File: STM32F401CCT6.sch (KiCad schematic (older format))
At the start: 42 parts, among them J1 USB_OTG, J2 Conn_02x03_Odd_Even, J3 Conn_01x20_des, J4 Conn_01x05_desc, J5 Conn_01x20, SW1 SW_Push, U1 MIC5219-3.3, U3 USBLC6-2SC6, Y1 32.786K, Y2 8MHz

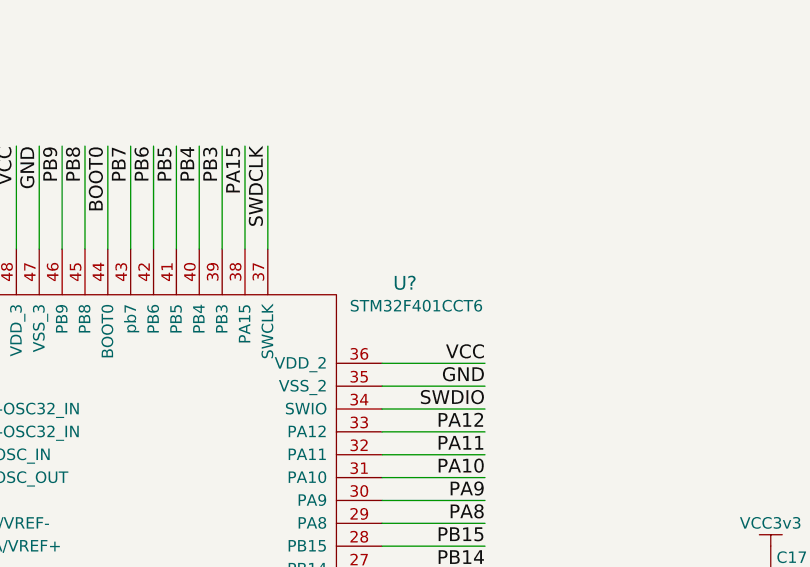
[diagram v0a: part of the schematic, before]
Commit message: Fixed the pad near tracks error (reallocated the QFN)
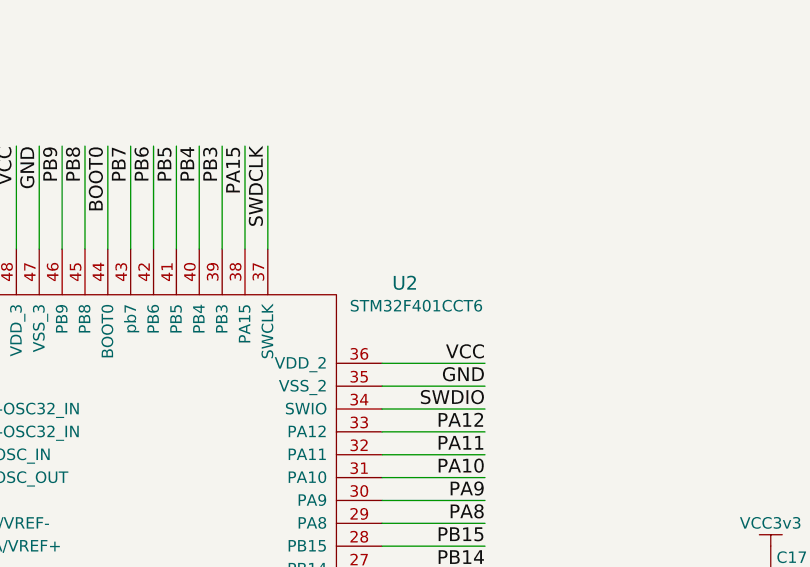
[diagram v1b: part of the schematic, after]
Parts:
- gave numbers to parts that had none: 1
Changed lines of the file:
@@
 $EndComp
 $Comp
-L GND #PWR01
+L GND #PWR9
 U 1 1 59D25E0A
 P 2500 1550
-F 0 "#PWR01" H 2500 1300 50  0001 C CNN
+F 0 "#PWR9" H 2500 1300 50  0001 C CNN
 F 1 "GND" H 2500 1400 50  0000 C CNN
 F 2 "" H 2500 1550 50  0001 C CNN
@@
 $EndComp
 $Comp
-L VCC3v3 #PWR02
+L VCC3v3 #PWR16
 U 1 1 59D2614B
 P 4700 850
-F 0 "#PWR02" H 4700 700 50  0001 C CNN
+F 0 "#PWR16" H 4700 700 50  0001 C CNN
 F 1 "VCC3v3" H 4700 950 50  0000 C CNN
 F 2 "" H 4700 850 50  0001 C CNN
@@
 $EndComp
 $Comp
-L VCC3v3 #PWR03
+L VCC3v3 #PWR17
 U 1 1 59D261AF
 P 4700 1350
-F 0 "#PWR03" H 4700 1200 50  0001 C CNN
+F 0 "#PWR17" H 4700 1200 50  0001 C CNN
 F 1 "VCC3v3" H 4700 1450 50  0000 C CNN
 F 2 "" H 4700 1350 50  0001 C CNN
@@
 $EndComp
 $Comp
-L VCC3v3 #PWR04
+L VCC3v3 #PWR13
 U 1 1 59D261DA
 P 3000 900
-F 0 "#PWR04" H 3000 750 50  0001 C CNN
+F 0 "#PWR13" H 3000 750 50  0001 C CNN
 F 1 "VCC3v3" H 3000 1000 50  0000 C CNN
 F 2 "" H 3000 900 50  0001 C CNN
@@
 BOOT0
 $Comp
-L VCC3v3 #PWR05
+L VCC3v3 #PWR2
 U 1 1 59D2665A
 P 1050 900
-F 0 "#PWR05" H 1050 750 50  0001 C CNN
+F 0 "#PWR2" H 1050 750 50  0001 C CNN
 F 1 "VCC3v3" H 1050 1000 50  0000 C CNN
 F 2 "" H 1050 900 50  0001 C CNN
@@
 RESET
 $Comp
-L GND #PWR06
+L GND #PWR3
 U 1 1 59D2716C
 P 1050 1950
-F 0 "#PWR06" H 1050 1700 50  0001 C CNN
+F 0 "#PWR3" H 1050 1700 50  0001 C CNN
 F 1 "GND" H 1050 1800 50  0000 C CNN
 F 2 "" H 1050 1950 50  0001 C CNN
@@
 $EndComp
 $Comp
-L 5V #PWR07
+L 5V #PWR6
 U 1 1 59D2797D
 P 1700 5900
-F 0 "#PWR07" H 1700 5750 50  0001 C CNN
+F 0 "#PWR6" H 1700 5750 50  0001 C CNN
 F 1 "5V" H 1700 6040 50  0000 C CNN
 F 2 "" H 1700 5900 50  0001 C CNN
@@
 $EndComp
 $Comp
-L VCC3v3 #PWR08
+L VCC3v3 #PWR7
 U 1 1 59D27D4D
 P 2150 6900
-F 0 "#PWR08" H 2150 6750 50  0001 C CNN
+F 0 "#PWR7" H 2150 6750 50  0001 C CNN
 F 1 "VCC3v3" H 2150 7000 50  0000 C CNN
 F 2 "" H 2150 6900 50  0001 C CNN
@@
 $EndComp
 $Comp
-L GND #PWR09
+L GND #PWR15
 U 1 1 59D289B6
 P 3750 5700
-F 0 "#PWR09" H 3750 5450 50  0001 C CNN
+F 0 "#PWR15" H 3750 5450 50  0001 C CNN
 F 1 "GND" H 3750 5550 50  0000 C CNN
 F 2 "" H 3750 5700 50  0001 C CNN
@@
 $EndComp
 $Comp
-L VCC3v3 #PWR010
+L VCC3v3 #PWR28
 U 1 1 59D28DD5
 P 10200 5450
-F 0 "#PWR010" H 10200 5300 50  0001 C CNN
+F 0 "#PWR28" H 10200 5300 50  0001 C CNN
 F 1 "VCC3v3" H 10200 5550 50  0000 C CNN
 F 2 "" H 10200 5450 50  0001 C CNN
@@
 $EndComp
 $Comp
-L GND #PWR011
+L GND #PWR29
 U 1 1 59D28EE2
 P 10200 5950
-F 0 "#PWR011" H 10200 5700 50  0001 C CNN
+F 0 "#PWR29" H 10200 5700 50  0001 C CNN
 F 1 "GND" H 10200 5800 50  0000 C CNN
 F 2 "" H 10200 5950 50  0001 C CNN
@@
 $EndComp
 $Comp
-L VCC3v3 #PWR012
+L VCC3v3 #PWR26
 U 1 1 59D2CC11
 P 9850 4400
-F 0 "#PWR012" H 9850 4250 50  0001 C CNN
+F 0 "#PWR26" H 9850 4250 50  0001 C CNN
 F 1 "VCC3v3" H 9850 4500 50  0000 C CNN
 F 2 "" H 9850 4400 50  0001 C CNN
@@
 $EndComp
 $Comp
-L GND #PWR013
+L GND #PWR27
 U 1 1 59D2CC17
 P 9850 4700
-F 0 "#PWR013" H 9850 4450 50  0001 C CNN
+F 0 "#PWR27" H 9850 4450 50  0001 C CNN
 F 1 "GND" H 9850 4550 50  0000 C CNN
 F 2 "" H 9850 4700 50  0001 C CNN
@@
 $EndComp
 $Comp
-L VCC3v3 #PWR014
+L VCC3v3 #PWR30
 U 1 1 59D2CC94
 P 10300 4400
-F 0 "#PWR014" H 10300 4250 50  0001 C CNN
+F 0 "#PWR30" H 10300 4250 50  0001 C CNN
 F 1 "VCC3v3" H 10300 4500 50  0000 C CNN
 F 2 "" H 10300 4400 50  0001 C CNN
@@
 $EndComp
 $Comp
-L GND #PWR015
+L GND #PWR31
 U 1 1 59D2CC9A
 P 10300 4700
-F 0 "#PWR015" H 10300 4450 50  0001 C CNN
+F 0 "#PWR31" H 10300 4450 50  0001 C CNN
 F 1 "GND" H 10300 4550 50  0000 C CNN
 F 2 "" H 10300 4700 50  0001 C CNN
@@
 $EndComp
 $Comp
-L GND #PWR016
+L GND #PWR5
 U 1 1 59D2D880
 P 1650 6750
-F 0 "#PWR016" H 1650 6500 50  0001 C CNN
+F 0 "#PWR5" H 1650 6500 50  0001 C CNN
 F 1 "GND" H 1650 6600 50  0000 C CNN
 F 2 "" H 1650 6750 50  0001 C CNN
@@
 $EndComp
 $Comp
-L GND #PWR017
+L GND #PWR1
 U 1 1 59D37486
 P 750 4400
-F 0 "#PWR017" H 750 4150 50  0001 C CNN
+F 0 "#PWR1" H 750 4150 50  0001 C CNN
 F 1 "GND" H 750 4250 50  0000 C CNN
 F 2 "" H 750 4400 50  0001 C CNN
@@
 $EndComp
 $Comp
-L 5V #PWR018
+L 5V #PWR4
 U 1 1 59D374F7
 P 1300 3500
-F 0 "#PWR018" H 1300 3350 50  0001 C CNN
+F 0 "#PWR4" H 1300 3350 50  0001 C CNN
 F 1 "5V" H 1300 3640 50  0000 C CNN
 F 2 "" H 1300 3500 50  0001 C CNN
@@
 $EndComp
 $Comp
-L VCC3v3 #PWR019
+L VCC3v3 #PWR10
 U 1 1 59D376BC
 P 2600 3550
-F 0 "#PWR019" H 2600 3400 50  0001 C CNN
+F 0 "#PWR10" H 2600 3400 50  0001 C CNN
 F 1 "VCC3v3" H 2600 3650 50  0000 C CNN
 F 2 "" H 2600 3550 50  0001 C CNN
@@
 $EndComp
 $Comp
-L GND #PWR020
+L GND #PWR11
 U 1 1 59D37C81
 P 2600 4350
-F 0 "#PWR020" H 2600 4100 50  0001 C CNN
+F 0 "#PWR11" H 2600 4100 50  0001 C CNN
 F 1 "GND" H 2600 4200 50  0000 C CNN
 F 2 "" H 2600 4350 50  0001 C CNN
@@
 $EndComp
 $Comp
-L GND #PWR021
+L GND #PWR12
 U 1 1 59D37D1C
 P 2950 4350
-F 0 "#PWR021" H 2950 4100 50  0001 C CNN
+F 0 "#PWR12" H 2950 4100 50  0001 C CNN
 F 1 "GND" H 2950 4200 50  0000 C CNN
 F 2 "" H 2950 4350 50  0001 C CNN
@@
 $EndComp
 $Comp
-L GND #PWR022
+L GND #PWR21
 U 1 1 59D379C4
 P 8700 900
-F 0 "#PWR022" H 8700 650 50  0001 C CNN
+F 0 "#PWR21" H 8700 650 50  0001 C CNN
 F 1 "GND" H 8700 750 50  0000 C CNN
 F 2 "" H 8700 900 50  0001 C CNN
@@
 $EndComp
 $Comp
-L VCC3v3 #PWR023
+L VCC3v3 #PWR14
 U 1 1 59D3C6B3
 P 3250 6850
-F 0 "#PWR023" H 3250 6700 50  0001 C CNN
+F 0 "#PWR14" H 3250 6700 50  0001 C CNN
 F 1 "VCC3v3" H 3250 6950 50  0000 C CNN
 F 2 "" H 3250 6850 50  0001 C CNN
@@
 $EndComp
 $Comp
-L GND #PWR024
+L GND #PWR8
 U 1 1 59D3C918
 P 2450 6850
-F 0 "#PWR024" H 2450 6600 50  0001 C CNN
+F 0 "#PWR8" H 2450 6600 50  0001 C CNN
 F 1 "GND" H 2450 6700 50  0000 C CNN
 F 2 "" H 2450 6850 50  0001 C CNN
@@
 PB11/VCAP1
 $Comp
-L GND #PWR025
+L GND #PWR18
 U 1 1 59FD831D
 P 6450 6150
-F 0 "#PWR025" H 6450 5900 50  0001 C CNN
+F 0 "#PWR18" H 6450 5900 50  0001 C CNN
 F 1 "GND" H 6450 6000 50  0000 C CNN
 F 2 "" H 6450 6150 50  0001 C CNN
@@
 $EndComp
 $Comp
-L VCC3v3 #PWR026
+L VCC3v3 #PWR19
 U 1 1 5A0064CD
 P 8400 5450
-F 0 "#PWR026" H 8400 5300 50  0001 C CNN
+F 0 "#PWR19" H 8400 5300 50  0001 C CNN
 F 1 "VCC3v3" H 8400 5550 50  0000 C CNN
 F 2 "" H 8400 5450 50  0001 C CNN
@@
 $EndComp
 $Comp
-L GND #PWR027
+L GND #PWR20
 U 1 1 5A0064D3
 P 8400 5950
-F 0 "#PWR027" H 8400 5700 50  0001 C CNN
+F 0 "#PWR20" H 8400 5700 50  0001 C CNN
 F 1 "GND" H 8400 5800 50  0000 C CNN
 F 2 "" H 8400 5950 50  0001 C CNN
@@
 $EndComp
 $Comp
-L VCC3v3 #PWR028
+L VCC3v3 #PWR24
 U 1 1 5A006C48
 P 9350 4400
-F 0 "#PWR028" H 9350 4250 50  0001 C CNN
+F 0 "#PWR24" H 9350 4250 50  0001 C CNN
 F 1 "VCC3v3" H 9350 4500 50  0000 C CNN
 F 2 "" H 9350 4400 50  0001 C CNN
@@
 $EndComp
 $Comp
-L GND #PWR029
+L GND #PWR25
 U 1 1 5A006C4E
 P 9350 4700
-F 0 "#PWR029" H 9350 4450 50  0001 C CNN
+F 0 "#PWR25" H 9350 4450 50  0001 C CNN
 F 1 "GND" H 9350 4550 50  0000 C CNN
 F 2 "" H 9350 4700 50  0001 C CNN
@@
 $EndComp
 $Comp
-L VCC3v3 #PWR030
+L VCC3v3 #PWR22
 U 1 1 5A006D31
 P 8850 4400
-F 0 "#PWR030" H 8850 4250 50  0001 C CNN
+F 0 "#PWR22" H 8850 4250 50  0001 C CNN
 F 1 "VCC3v3" H 8850 4500 50  0000 C CNN
 F 2 "" H 8850 4400 50  0001 C CNN
@@
 $EndComp
 $Comp
-L GND #PWR031
+L GND #PWR23
 U 1 1 5A006D37
 P 8850 4700
-F 0 "#PWR031" H 8850 4450 50  0001 C CNN
+F 0 "#PWR23" H 8850 4450 50  0001 C CNN
 F 1 "GND" H 8850 4550 50  0000 C CNN
 F 2 "" H 8850 4700 50  0001 C CNN
@@
 $EndComp
 $Comp
-L STM32F401CCT6 U?
+L STM32F401CCT6 U2
 U 1 1 5A00751A
 P 5700 3850
-F 0 "U?" H 7250 4450 60  0000 C CNN
+F 0 "U2" H 7250 4450 60  0000 C CNN
 F 1 "STM32F401CCT6" H 7300 4350 50  0000 C CNN
 F 2 "" H 5700 3850 60  0001 C CNN

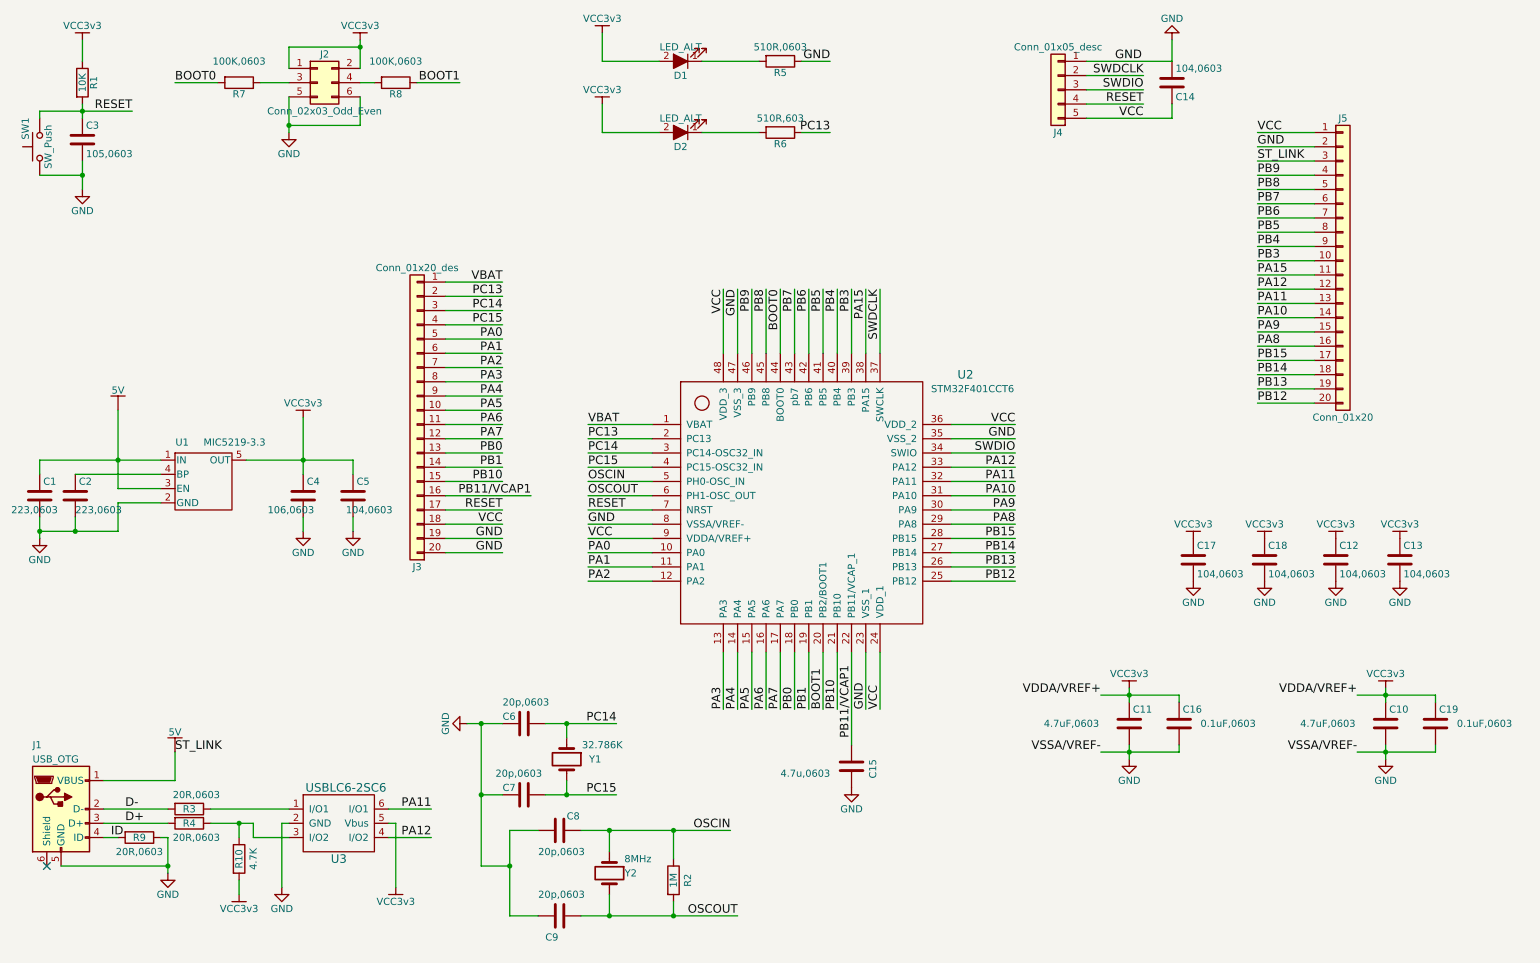
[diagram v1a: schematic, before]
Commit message: Change pin20 to Pwr Enable and added a resistor on it
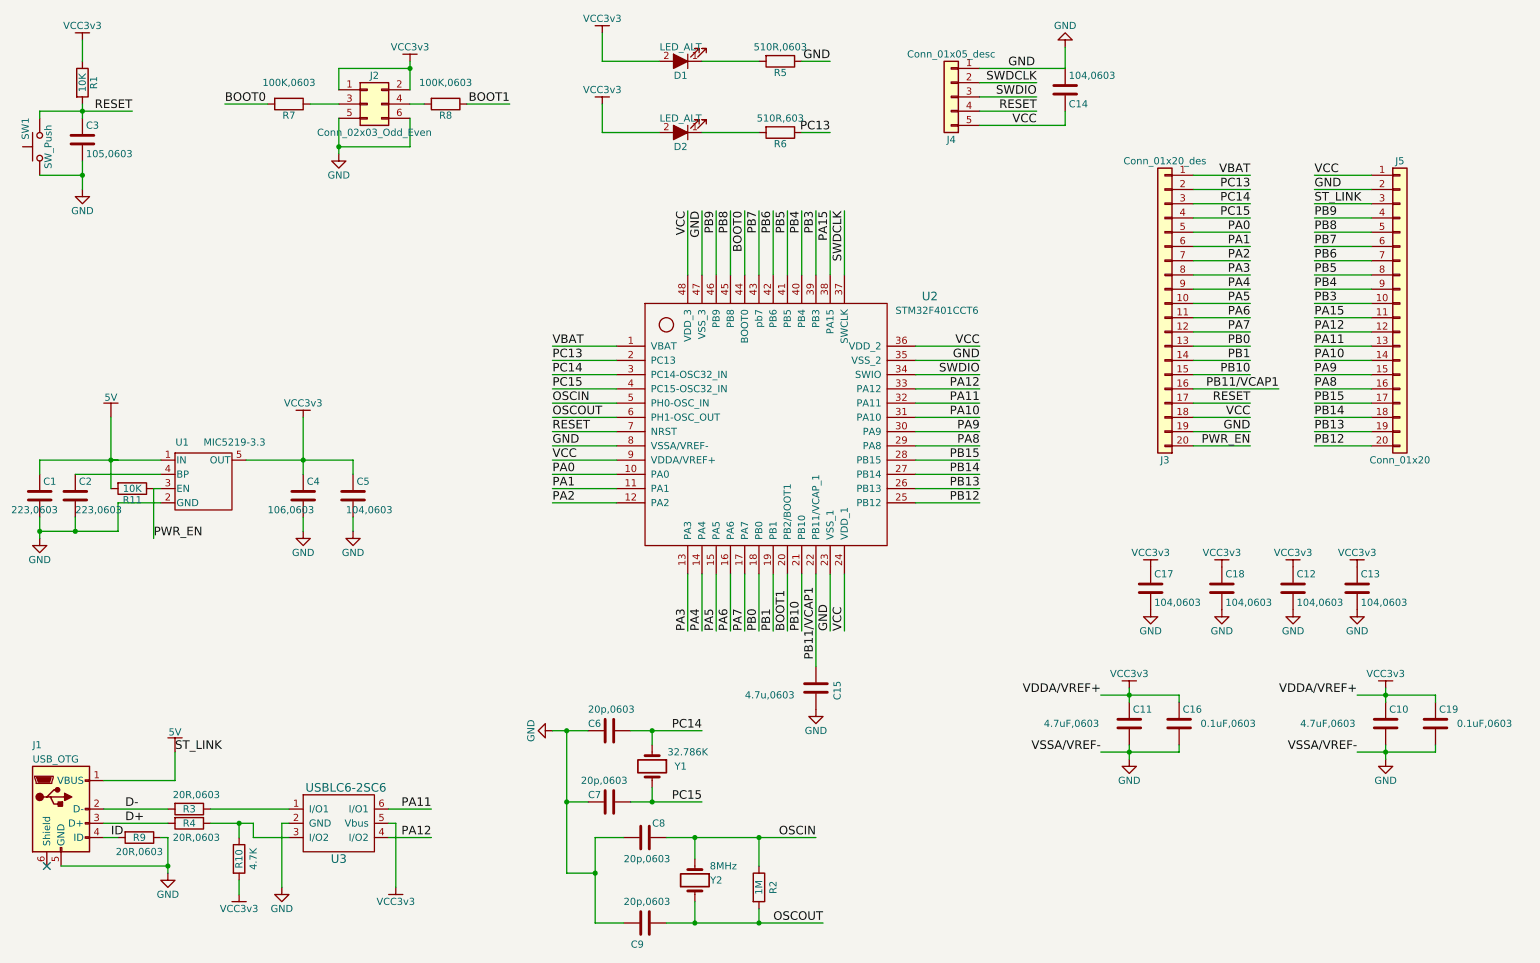
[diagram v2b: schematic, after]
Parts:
- added R11: 10K, Resistors_SMD:R_0603, symbol R
- U2: footprint (none) -> QFPN48:QFN_QFP48
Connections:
- net +5V: now also R11.2; no longer U1.3 (EN)
- net GND: no longer J3.20 (Pin_20)
- new net PWR_EN: J3.20 (Pin_20), R11.1, U1.3 (EN)
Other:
- moved on the sheet: C12, C13, C14, C15, C17, C18, C6, C7, C8, C9, J2, J3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

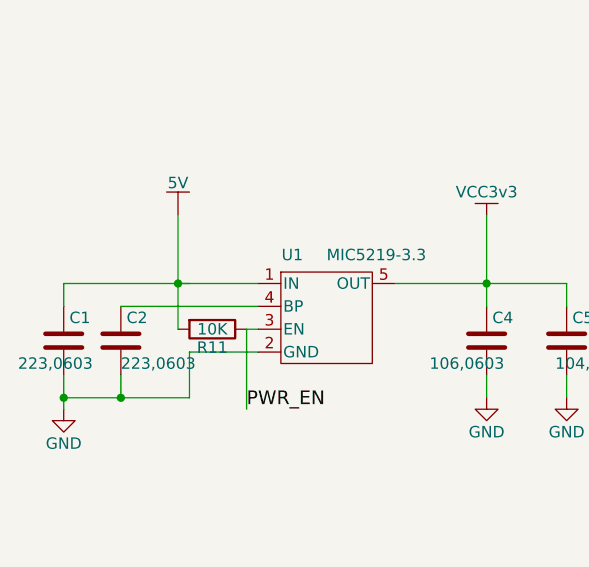
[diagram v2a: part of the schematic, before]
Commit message: Changed pin 20 to PWE schemaic
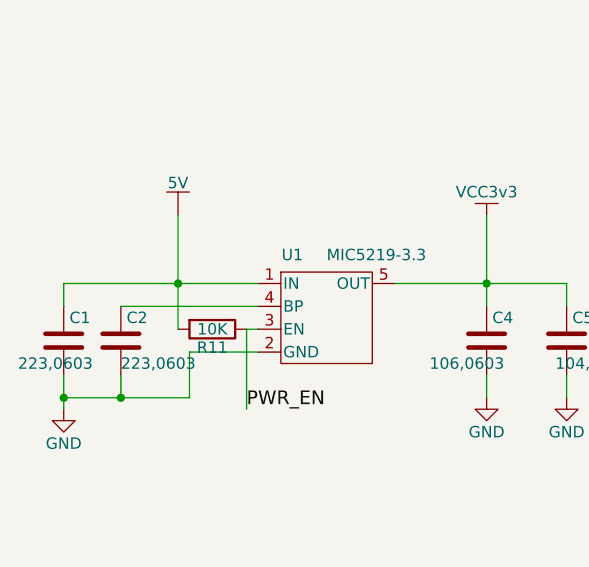
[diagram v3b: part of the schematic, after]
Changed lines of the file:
@@
 Wire Wire Line
 	1000 3950 1600 3950
-Wire Wire Line
-	750  3850 1600 3850
 Connection ~ 2600 3850
 Wire Wire Line
@@
 	1250 3550 1250 4050
 Wire Wire Line
-	1250 3850 1300 3850
+	750  3850 1600 3850
 Connection ~ 1250 3850
 Text Label 1550 4400 0    60   ~ 0

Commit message: Re-routed (prioritised D+ D- SWDIO SWCLK) by reducing the track length and via along the tracks.
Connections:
- net PA11: now also U3.1 (I/O1); no longer U3.6 (I/O1)
- net PA12: now also U3.3 (I/O2); no longer U3.4 (I/O2)
- net at R3.1: now also U3.6 (I/O1); no longer U3.1 (I/O1)
- net at R10.1, R4.1: now also U3.4 (I/O2); no longer U3.3 (I/O2)
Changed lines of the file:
@@
 L USBLC6-2SC6 U3
 U 1 1 59D3A2F4
-P 2950 6500
-F 0 "U3" H 2850 6350 60  0000 C CNN
-F 1 "USBLC6-2SC6" H 2900 6850 60  0000 C CNN
-F 2 "TO_SOT_Packages_SMD:SOT-23-6" H 2950 6500 60  0001 C CNN
-F 3 "" H 2950 6500 60  0001 C CNN
-	1    2950 6500
-	1    0    0    -1
-$EndComp
-$Comp
-L VCC3v3 #PWR023
-U 1 1 59D3C6B3
-P 3250 6850
-F 0 "#PWR023" H 3250 6700 50  0001 C CNN
-F 1 "VCC3v3" H 3250 6950 50  0000 C CNN
-F 2 "" H 3250 6850 50  0001 C CNN
-F 3 "" H 3250 6850 50  0001 C CNN
-	1    3250 6850
-	-1   0    0    1
-$EndComp
-$Comp
-L GND #PWR024
+P 2750 6500
+F 0 "U3" H 2650 6350 60  0000 C CNN
+F 1 "USBLC6-2SC6" H 2700 6850 60  0000 C CNN
+F 2 "TO_SOT_Packages_SMD:SOT-23-6" H 2750 6500 60  0001 C CNN
+F 3 "" H 2750 6500 60  0001 C CNN
+	1    2750 6500
+	-1   0    0    -1
+$EndComp
+$Comp
+L GND #PWR023
 U 1 1 59D3C918
-P 2450 6850
-F 0 "#PWR024" H 2450 6600 50  0001 C CNN
-F 1 "GND" H 2450 6700 50  0000 C CNN
-F 2 "" H 2450 6850 50  0001 C CNN
-F 3 "" H 2450 6850 50  0001 C CNN
-	1    2450 6850
+P 3250 6800
+F 0 "#PWR023" H 3250 6550 50  0001 C CNN
+F 1 "GND" H 3250 6650 50  0000 C CNN
+F 2 "" H 3250 6800 50  0001 C CNN
+F 3 "" H 3250 6800 50  0001 C CNN
+	1    3250 6800
 	1    0    0    -1
 $EndComp
@@
 	2450 6400 2450 6850
 Wire Wire Line
-	3250 6400 3250 6850
-Wire Wire Line
 	3200 6400 3250 6400
 Wire Wire Line
@@
 PB11/VCAP1
 $Comp
-L GND #PWR025
+L GND #PWR024
 U 1 1 59FD831D
 P 6200 5600
-F 0 "#PWR025" H 6200 5350 50  0001 C CNN
+F 0 "#PWR024" H 6200 5350 50  0001 C CNN
 F 1 "GND" H 6200 5450 50  0000 C CNN
 F 2 "" H 6200 5600 50  0001 C CNN
@@
 $EndComp
 $Comp
-L VCC3v3 #PWR026
+L VCC3v3 #PWR025
 U 1 1 5A0064CD
 P 8400 5450
-F 0 "#PWR026" H 8400 5300 50  0001 C CNN
+F 0 "#PWR025" H 8400 5300 50  0001 C CNN
 F 1 "VCC3v3" H 8400 5550 50  0000 C CNN
 F 2 "" H 8400 5450 50  0001 C CNN
@@
 $EndComp
 $Comp
-L GND #PWR027
+L GND #PWR026
 U 1 1 5A0064D3
 P 8400 5950
-F 0 "#PWR027" H 8400 5700 50  0001 C CNN
+F 0 "#PWR026" H 8400 5700 50  0001 C CNN
 F 1 "GND" H 8400 5800 50  0000 C CNN
 F 2 "" H 8400 5950 50  0001 C CNN
@@
 $EndComp
 $Comp
-L VCC3v3 #PWR028
+L VCC3v3 #PWR027
 U 1 1 5A006C48
 P 9050 4600
-F 0 "#PWR028" H 9050 4450 50  0001 C CNN
+F 0 "#PWR027" H 9050 4450 50  0001 C CNN
 F 1 "VCC3v3" H 9050 4700 50  0000 C CNN
 F 2 "" H 9050 4600 50  0001 C CNN
@@
 $EndComp
 $Comp
-L GND #PWR029
+L GND #PWR028
 U 1 1 5A006C4E
 P 9050 4900
-F 0 "#PWR029" H 9050 4650 50  0001 C CNN
+F 0 "#PWR028" H 9050 4650 50  0001 C CNN
 F 1 "GND" H 9050 4750 50  0000 C CNN
 F 2 "" H 9050 4900 50  0001 C CNN
@@
 $EndComp
 $Comp
-L VCC3v3 #PWR030
+L VCC3v3 #PWR029
 U 1 1 5A006D31
 P 8550 4600
-F 0 "#PWR030" H 8550 4450 50  0001 C CNN
+F 0 "#PWR029" H 8550 4450 50  0001 C CNN
 F 1 "VCC3v3" H 8550 4700 50  0000 C CNN
 F 2 "" H 8550 4600 50  0001 C CNN
@@
 $EndComp
 $Comp
-L GND #PWR031
+L GND #PWR030
 U 1 1 5A006D37
 P 8550 4900
-F 0 "#PWR031" H 8550 4650 50  0001 C CNN
+F 0 "#PWR030" H 8550 4650 50  0001 C CNN
 F 1 "GND" H 8550 4750 50  0000 C CNN
 F 2 "" H 8550 4900 50  0001 C CNN
@@
 Text Label 1550 4400 0    60   ~ 0
 PWR_EN
+Wire Wire Line
+	3250 6400 3250 6800
+Wire Wire Line
+	2450 6850 2150 6850
+Connection ~ 2150 6850
 $EndSCHEMATC
